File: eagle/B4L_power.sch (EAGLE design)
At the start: 22 parts, among them IC1 LM2576S, IC2 TL081CP, Q1 STP40NF03L

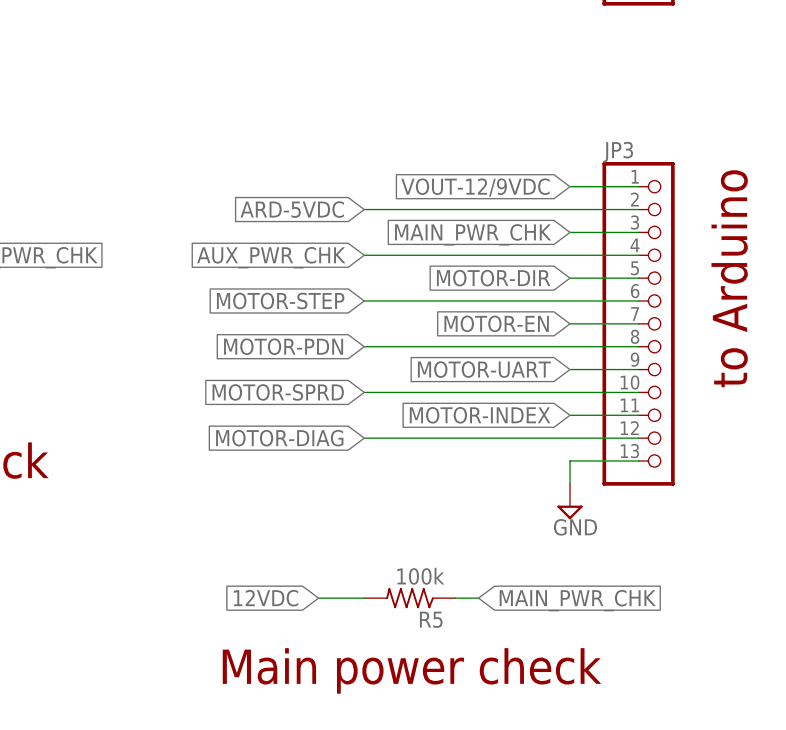
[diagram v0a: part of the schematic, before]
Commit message: Duplicate UART (for TX/RX on arduino)
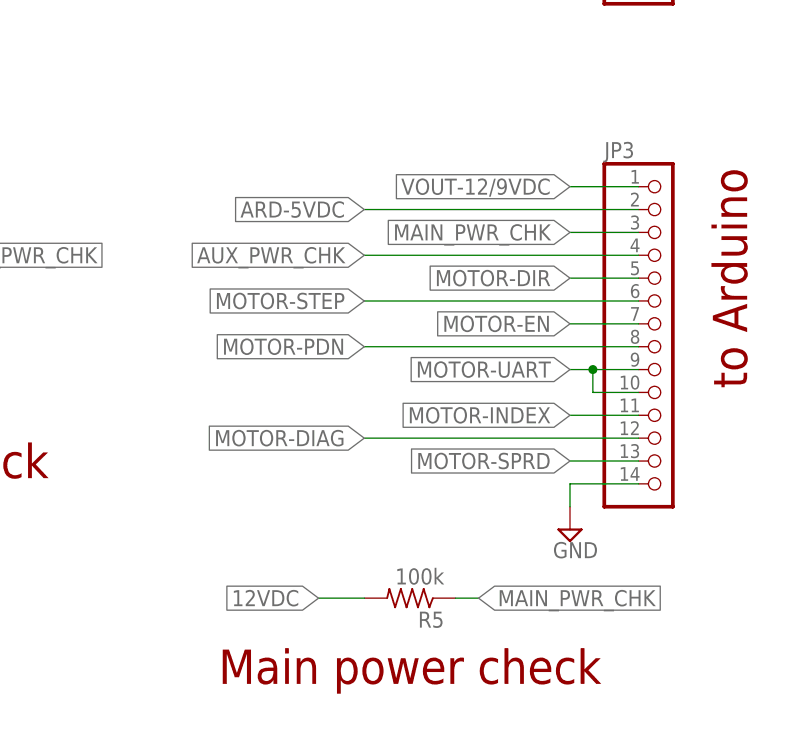
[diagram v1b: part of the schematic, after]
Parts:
- JP3: device pinhead:PINHD-1X13 -> pinhead:PINHD-1X14
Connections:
- net GND: now also JP3.14; no longer JP3.13
- net MOTOR-SPRD: now also JP3.13; no longer JP3.10
- net MOTOR-UART: now also JP3.10
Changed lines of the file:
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@@
 <part name="SUPPLY14" library="supply2" library_urn="urn:adsk.eagle:library:372" deviceset="GND" device=""/>
 <part name="SUPPLY15" library="supply2" library_urn="urn:adsk.eagle:library:372" deviceset="GND" device=""/>
-<part name="JP3" library="pinhead" library_urn="urn:adsk.eagle:library:325" deviceset="PINHD-1X13" device="" package3d_urn="urn:adsk.eagle:package:22421/2"/>
+<part name="JP3" library="pinhead" library_urn="urn:adsk.eagle:library:325" deviceset="PINHD-1X14" device="" package3d_urn="urn:adsk.eagle:package:22417/2"/>
 </parts>
 <sheets>
@@
 <attribute name="VALUE" x="232.41" y="124.46" size="1.778" layer="96"/>
 </instance>
-<instance part="SUPPLY10" gate="GND" x="228.6" y="71.12" smashed="yes">
-<attribute name="VALUE" x="226.695" y="67.945" size="1.778" layer="96"/>
+<instance part="SUPPLY10" gate="GND" x="228.6" y="68.58" smashed="yes">
+<attribute name="VALUE" x="226.695" y="65.405" size="1.778" layer="96"/>
 </instance>
 <instance part="JP4" gate="G$1" x="17.78" y="68.58" smashed="yes" rot="R180">
@@
 <instance part="JP3" gate="A" x="238.76" y="91.44" smashed="yes">
 <attribute name="NAME" x="232.41" y="109.855" size="1.778" layer="95"/>
-<attribute name="VALUE" x="232.41" y="71.12" size="1.778" layer="96"/>
+<attribute name="VALUE" x="232.41" y="68.58" size="1.778" layer="96"/>
 </instance>
 </instances>
@@
 <segment>
 <pinref part="SUPPLY10" gate="GND" pin="GND"/>
-<pinref part="JP3" gate="A" pin="13"/>
-<wire x1="228.6" y1="73.66" x2="228.6" y2="76.2" width="0.1524" layer="91"/>
-<wire x1="228.6" y1="76.2" x2="236.22" y2="76.2" width="0.1524" layer="91"/>
+<wire x1="228.6" y1="71.12" x2="228.6" y2="73.66" width="0.1524" layer="91"/>
+<pinref part="JP3" gate="A" pin="14"/>
+<wire x1="228.6" y1="73.66" x2="236.22" y2="73.66" width="0.1524" layer="91"/>
 </segment>
 </net>
@@
 </segment>
 <segment>
-<wire x1="236.22" y1="86.36" x2="228.6" y2="86.36" width="0.1524" layer="91"/>
+<wire x1="236.22" y1="86.36" x2="231.14" y2="86.36" width="0.1524" layer="91"/>
 <label x="228.6" y="86.36" size="1.778" layer="95" rot="R180" xref="yes"/>
 <pinref part="JP3" gate="A" pin="9"/>
+<pinref part="JP3" gate="A" pin="10"/>
+<wire x1="231.14" y1="86.36" x2="228.6" y2="86.36" width="0.1524" layer="91"/>
+<wire x1="236.22" y1="83.82" x2="231.14" y2="83.82" width="0.1524" layer="91"/>
+<wire x1="231.14" y1="83.82" x2="231.14" y2="86.36" width="0.1524" layer="91"/>
+<junction x="231.14" y="86.36"/>
 </segment>
 </net>
@@
 </segment>
 <segment>
-<pinref part="JP3" gate="A" pin="10"/>
-<wire x1="236.22" y1="83.82" x2="205.74" y2="83.82" width="0.1524" layer="91"/>
-<label x="205.74" y="83.82" size="1.778" layer="95" rot="R180" xref="yes"/>
+<pinref part="JP3" gate="A" pin="13"/>
+<wire x1="236.22" y1="76.2" x2="228.6" y2="76.2" width="0.1524" layer="91"/>
+<label x="228.6" y="76.2" size="1.778" layer="95" rot="R180" xref="yes"/>
 </segment>
 </net>
@@
 </segment>
 <segment>
-<pinref part="JP3" gate="A" pin="11"/>
 <wire x1="236.22" y1="81.28" x2="228.6" y2="81.28" width="0.1524" layer="91"/>
 <label x="228.6" y="81.28" size="1.778" layer="95" rot="R180" xref="yes"/>
+<pinref part="JP3" gate="A" pin="11"/>
 </segment>
 </net>
@@
 </segment>
 <segment>
-<pinref part="JP3" gate="A" pin="12"/>
 <wire x1="236.22" y1="78.74" x2="205.74" y2="78.74" width="0.1524" layer="91"/>
 <label x="205.74" y="78.74" size="1.778" layer="95" rot="R180" xref="yes"/>
-</segment>
-</net>
+<pinref part="JP3" gate="A" pin="12"/>
+</segment>
+</net>

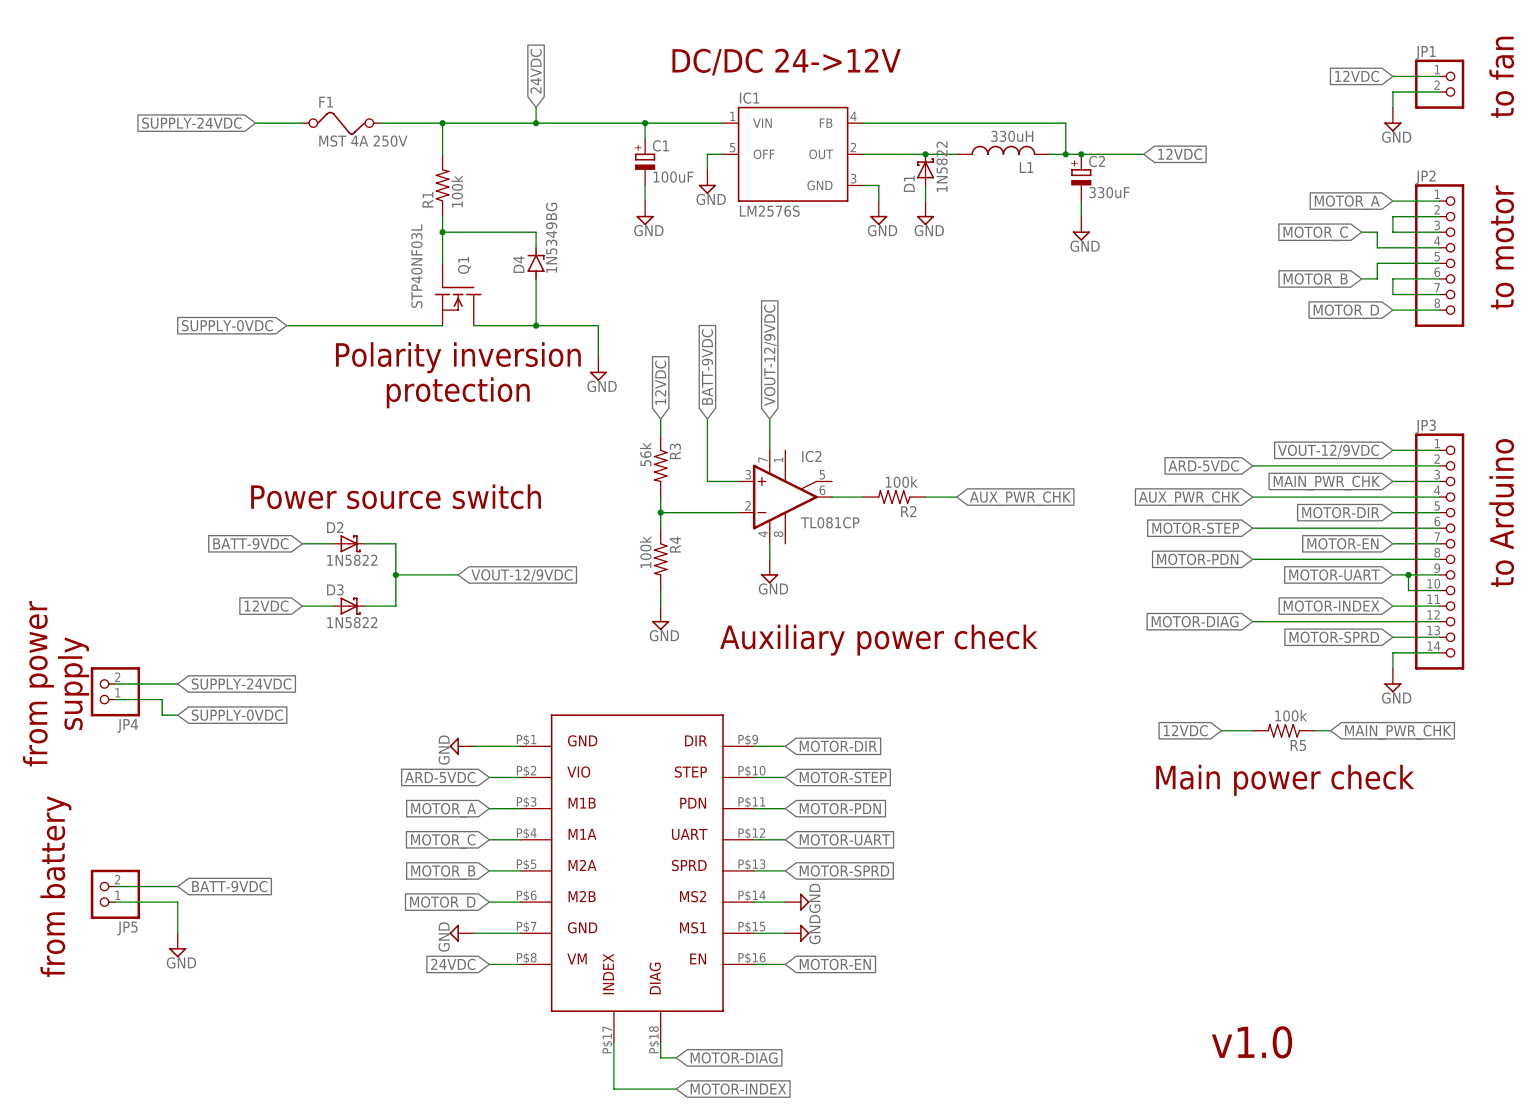
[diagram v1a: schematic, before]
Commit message: Power board update to 48V
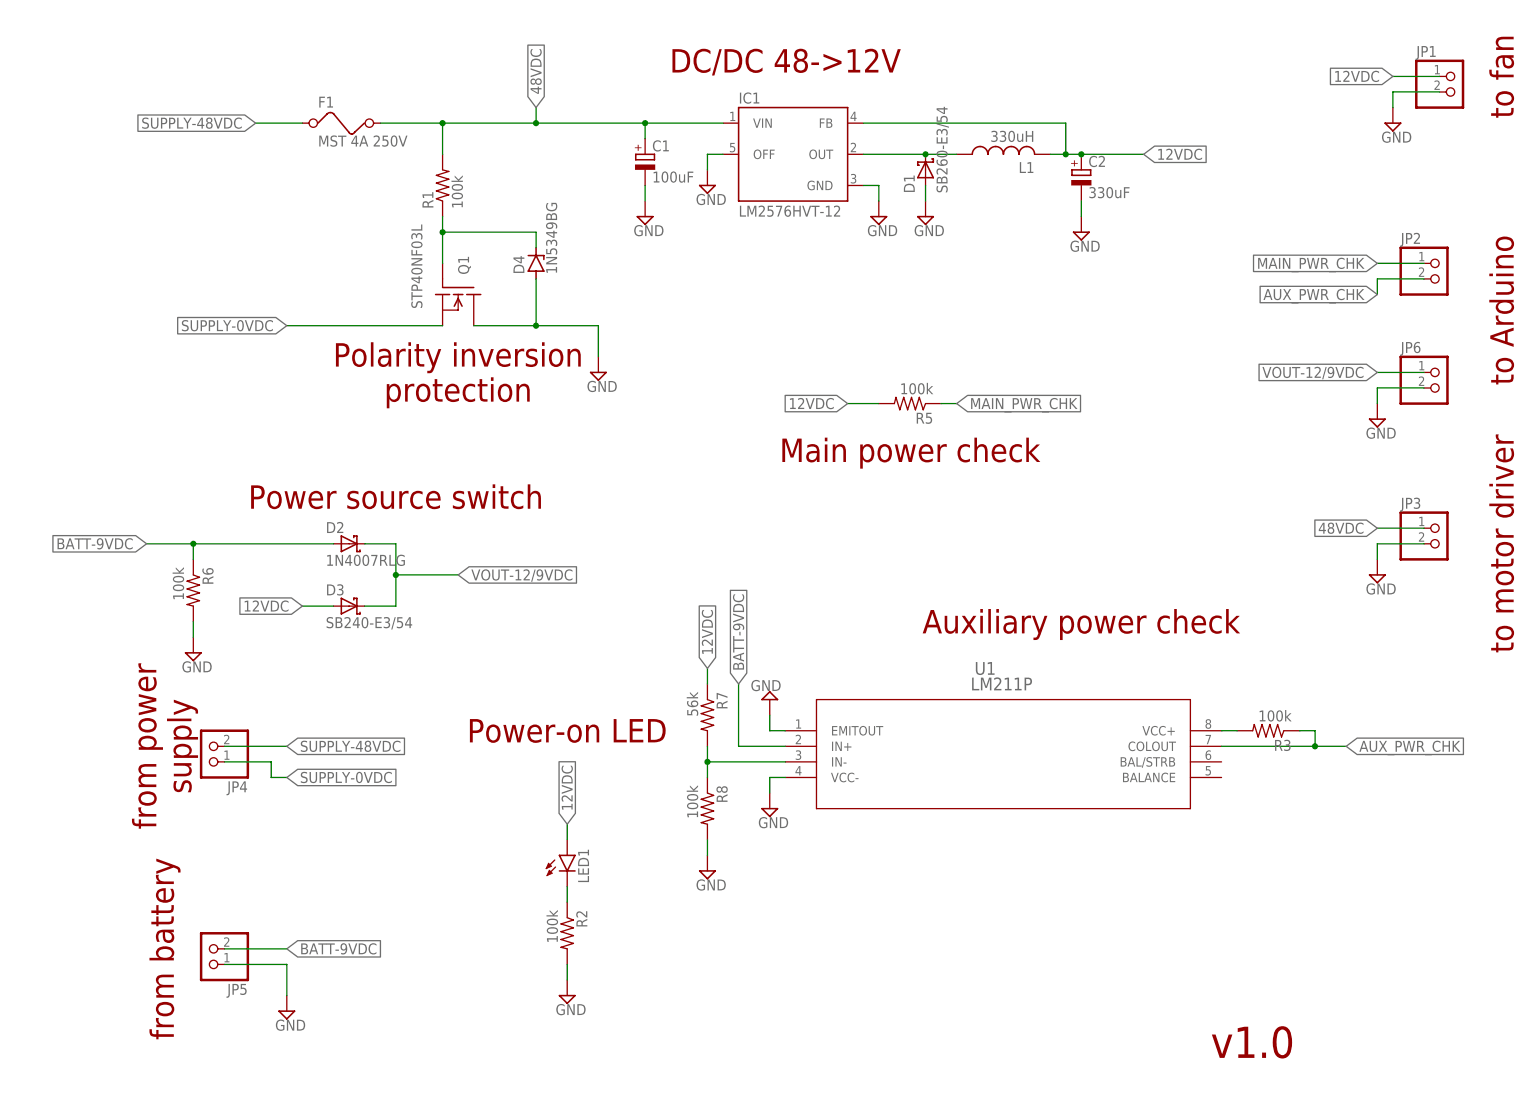
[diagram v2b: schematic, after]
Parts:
- removed IC2: TL081CP, linear:TL081P
- removed R4: 100k, rcl:R-US_0309/10
- removed U$1: TMC2209-SILENTSTEPSTICK, custom:TMC2209-SILENTSTEPSTICK
- added JP6: (no value), pinhead:PINHD-1X2
- added LED1: (no value), led:LED5MM
- added R6, R8: 100k, rcl:R-US_0309/10
- added R7: 56k, rcl:R-US_0309/10
- added U1: LM211P, custom:LM211P
- D1: value 1N5822 -> SB260-E3/54
- D2: value 1N5822 -> 1N4007RLG
- D3: value 1N5822 -> SB240-E3/54
- IC1: value LM2576S -> LM2576HVT-12
- JP2: device pinhead:PINHD-1X8 -> pinhead:PINHD-1X2
- JP3: device pinhead:PINHD-1X14 -> pinhead:PINHD-1X2
- R3: value 56k -> 100k
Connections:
- net SUPPLY-24VDC renamed SUPPLY-48VDC
- removed net 24VDC: C1.+, F1.2, IC1.VIN, R1.2, U$1.P$8
- removed net ARD-5VDC: JP3.2, U$1.P$2
- removed net MOTOR-DIAG: JP3.12, U$1.P$18
- removed net MOTOR-DIR: JP3.5, U$1.P$9
- removed net MOTOR-EN: JP3.7, U$1.P$16
- removed net MOTOR-INDEX: JP3.11, U$1.P$17
- removed net MOTOR-PDN: JP3.8, U$1.P$11
- removed net MOTOR-SPRD: JP3.13, U$1.P$13
- removed net MOTOR-STEP: JP3.6, U$1.P$10
- removed net MOTOR-UART: JP3.10, JP3.9, U$1.P$12
- removed net MOTOR_A: JP2.1, U$1.P$3
- removed net MOTOR_B: JP2.5, U$1.P$5
- removed net MOTOR_C: JP2.4, U$1.P$4
- removed net MOTOR_D: JP2.8, U$1.P$6
- removed net N$12: JP2.6, JP2.7
- removed net N$5: IC2.OUT, R2.2
- removed net N$8: JP2.2, JP2.3
- new net 48VDC: C1.+, F1.2, IC1.VIN, JP3.1, R1.2
- new net N$4: R3.2, U1.VCC+
- new net N$6: R7.2, R8.1, U1.IN-
- net 12VDC: now also LED1.A, R7.1; no longer R3.1
- net AUX_PWR_CHK: now also JP2.2, R3.1, U1.COLOUT; no longer JP3.4, R2.1
- net BATT-9VDC: now also R6.1, U1.IN+; no longer IC2.+IN
- net GND: now also JP3.2, JP6.2, R2.2, R6.2, R8.2, U1.EMITOUT, U1.VCC-; no longer IC2.V-, JP3.14, R4.2, U$1.P$1, U$1.P$14, U$1.P$15, U$1.P$7
- net MAIN_PWR_CHK: now also JP2.1; no longer JP3.3
- net N$3: now also LED1.C, R2.1; no longer IC2.-IN, R3.2, R4.1
- net VOUT-12/9VDC: now also JP6.1; no longer IC2.V+, JP3.1
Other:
- note added: "DC/DC 48->12V"
- note added: "Power-on LED"
- note added: "to motor driver"
- note removed: "DC/DC 24->12V"
- note removed: "to motor"
- moved on the sheet: JP4, JP5, R2, R3, R5

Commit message: Create power board BOM
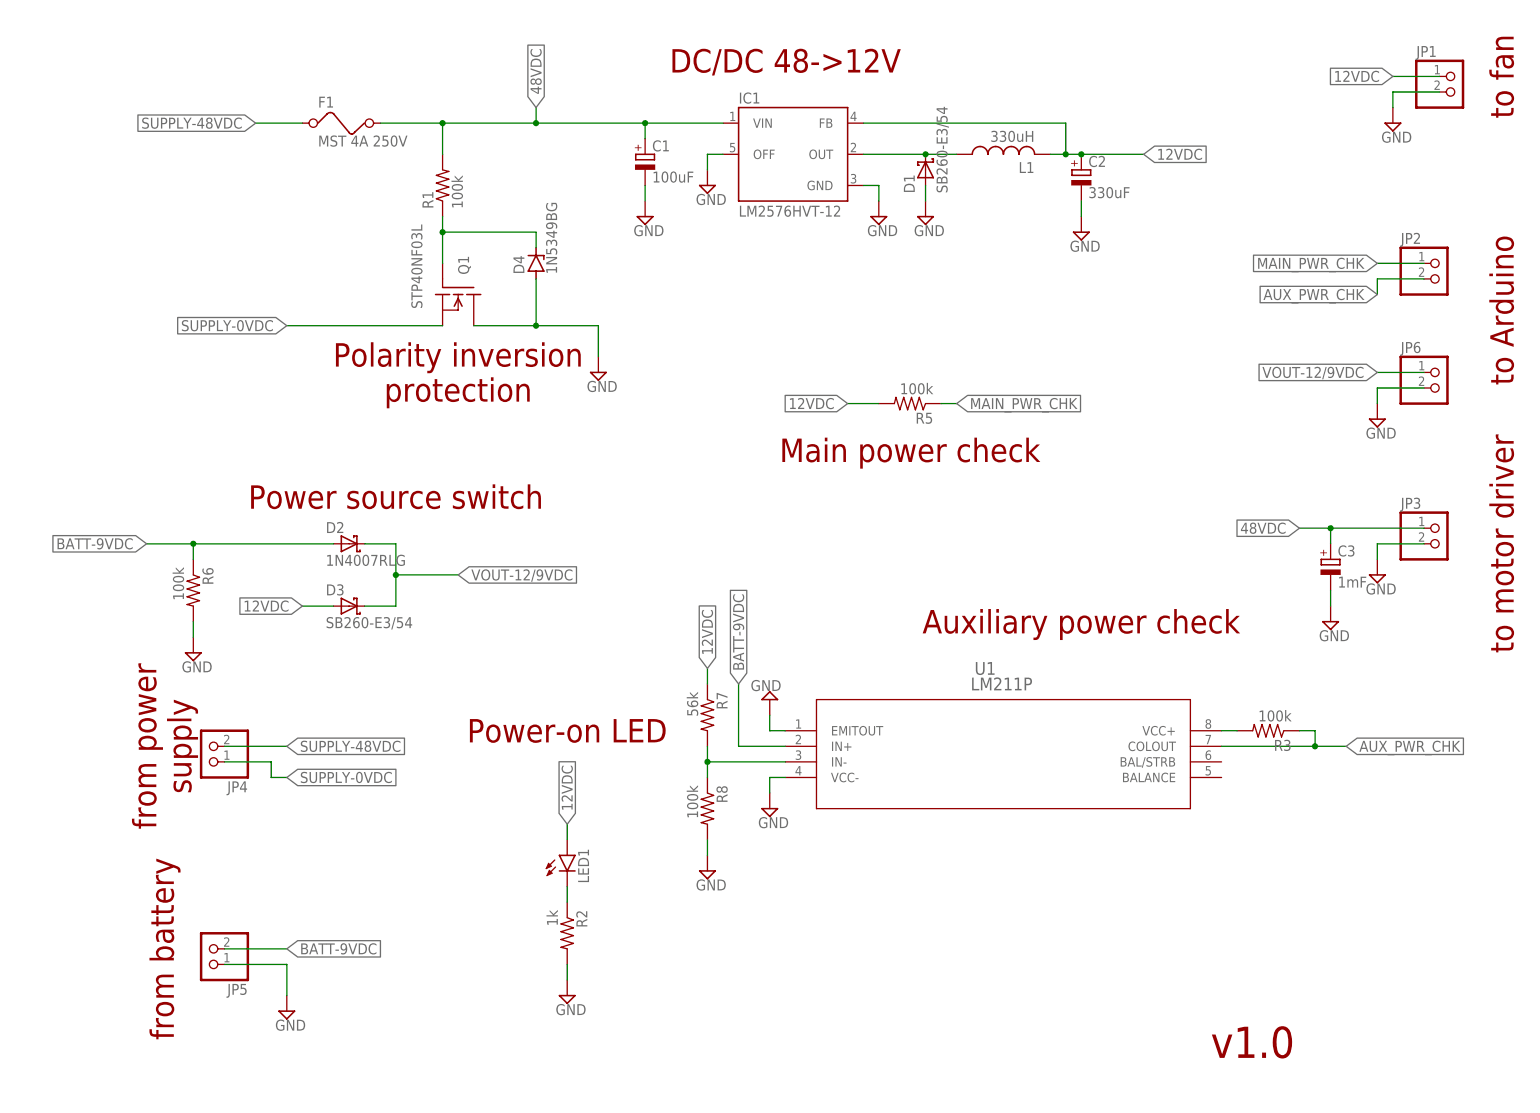
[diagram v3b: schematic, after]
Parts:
- added C3: 1mF, rcl:CPOL-EU140CLH-1010
- D3: value SB240-E3/54 -> SB260-E3/54
- R2: value 100k -> 1k
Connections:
- net 48VDC: now also C3.+
- net GND: now also C3.-
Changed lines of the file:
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@@
 <part name="F1" library="special" library_urn="urn:adsk.eagle:library:367" deviceset="FUSE" device="" package3d_urn="urn:adsk.eagle:package:26650/1" value="MST 4A 250V"/>
 <part name="D2" library="1N5822" deviceset="1N5822" device="" value="1N4007RLG"/>
-<part name="D3" library="1N5822" deviceset="1N5822" device="" value="SB240-E3/54"/>
+<part name="D3" library="1N5822" deviceset="1N5822" device="" value="SB260-E3/54"/>
 <part name="Q1" library="transistor-fet" library_urn="urn:adsk.eagle:library:396" deviceset="BUZ10" device="" package3d_urn="urn:adsk.eagle:package:28520/1" value="STP40NF03L"/>
 <part name="R1" library="rcl" library_urn="urn:adsk.eagle:library:334" deviceset="R-US_" device="0309/10" package3d_urn="urn:adsk.eagle:package:23567/2" value="100k"/>
@@
 <part name="R3" library="rcl" library_urn="urn:adsk.eagle:library:334" deviceset="R-US_" device="0309/10" package3d_urn="urn:adsk.eagle:package:23567/2" value="100k"/>
 <part name="SUPPLY7" library="supply2" library_urn="urn:adsk.eagle:library:372" deviceset="GND" device=""/>
-<part name="R2" library="rcl" library_urn="urn:adsk.eagle:library:334" deviceset="R-US_" device="0309/10" package3d_urn="urn:adsk.eagle:package:23567/2" value="100k"/>
+<part name="R2" library="rcl" library_urn="urn:adsk.eagle:library:334" deviceset="R-US_" device="0309/10" package3d_urn="urn:adsk.eagle:package:23567/2" value="1k"/>
 <part name="SUPPLY8" library="supply2" library_urn="urn:adsk.eagle:library:372" deviceset="GND" device=""/>
 <part name="LED1" library="led" library_urn="urn:adsk.eagle:library:259" deviceset="LED" device="5MM" package3d_urn="urn:adsk.eagle:package:15799/2"/>
+<part name="C3" library="rcl" library_urn="urn:adsk.eagle:library:334" deviceset="CPOL-EU" device="140CLH-1010" package3d_urn="urn:adsk.eagle:package:23391/2" value="1mF"/>
+<part name="SUPPLY16" library="supply2" library_urn="urn:adsk.eagle:library:372" deviceset="GND" device=""/>
 </parts>
 <sheets>
@@
 <attribute name="VALUE" x="99.695" y="36.068" size="1.778" layer="96" rot="R90"/>
 </instance>
+<instance part="C3" gate="G$1" x="218.44" y="88.9" smashed="yes">
+<attribute name="NAME" x="219.583" y="89.3826" size="1.778" layer="95"/>
+<attribute name="VALUE" x="219.583" y="84.3026" size="1.778" layer="96"/>
+</instance>
+<instance part="SUPPLY16" gate="GND" x="218.44" y="78.74" smashed="yes">
+<attribute name="VALUE" x="216.535" y="75.565" size="1.778" layer="96"/>
+</instance>
 </instances>
 <busses>
@@
 <wire x1="93.98" y1="20.32" x2="93.98" y2="22.86" width="0.1524" layer="91"/>
 </segment>
+<segment>
+<pinref part="C3" gate="G$1" pin="-"/>
+<pinref part="SUPPLY16" gate="GND" pin="GND"/>
+<wire x1="218.44" y1="83.82" x2="218.44" y2="81.28" width="0.1524" layer="91"/>
+</segment>
 </net>
 <net name="VOUT-12/9VDC" class="0">
@@
 <segment>
 <pinref part="JP3" gate="G$1" pin="1"/>
-<wire x1="233.68" y1="93.98" x2="226.06" y2="93.98" width="0.1524" layer="91"/>
-<label x="226.06" y="93.98" size="1.778" layer="95" rot="R180" xref="yes"/>
-</segment>
-<segment>
+<wire x1="233.68" y1="93.98" x2="218.44" y2="93.98" width="0.1524" layer="91"/>
+<label x="213.36" y="93.98" size="1.778" layer="95" rot="R180" xref="yes"/>
+<pinref part="C3" gate="G$1" pin="+"/>
+<wire x1="218.44" y1="93.98" x2="213.36" y2="93.98" width="0.1524" layer="91"/>
+<wire x1="218.44" y1="91.44" x2="218.44" y2="93.98" width="0.1524" layer="91"/>
+<junction x="218.44" y="93.98"/>
+</segment>
+<segment>
